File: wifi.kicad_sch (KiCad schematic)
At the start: 24 parts, among them P2 USB_C_Receptacle_USB2.0_16P, Q1 2N7002, U7 SC16C550BIBS, U8 ESP32-C3-WROOM-02, Y1 24 MHz

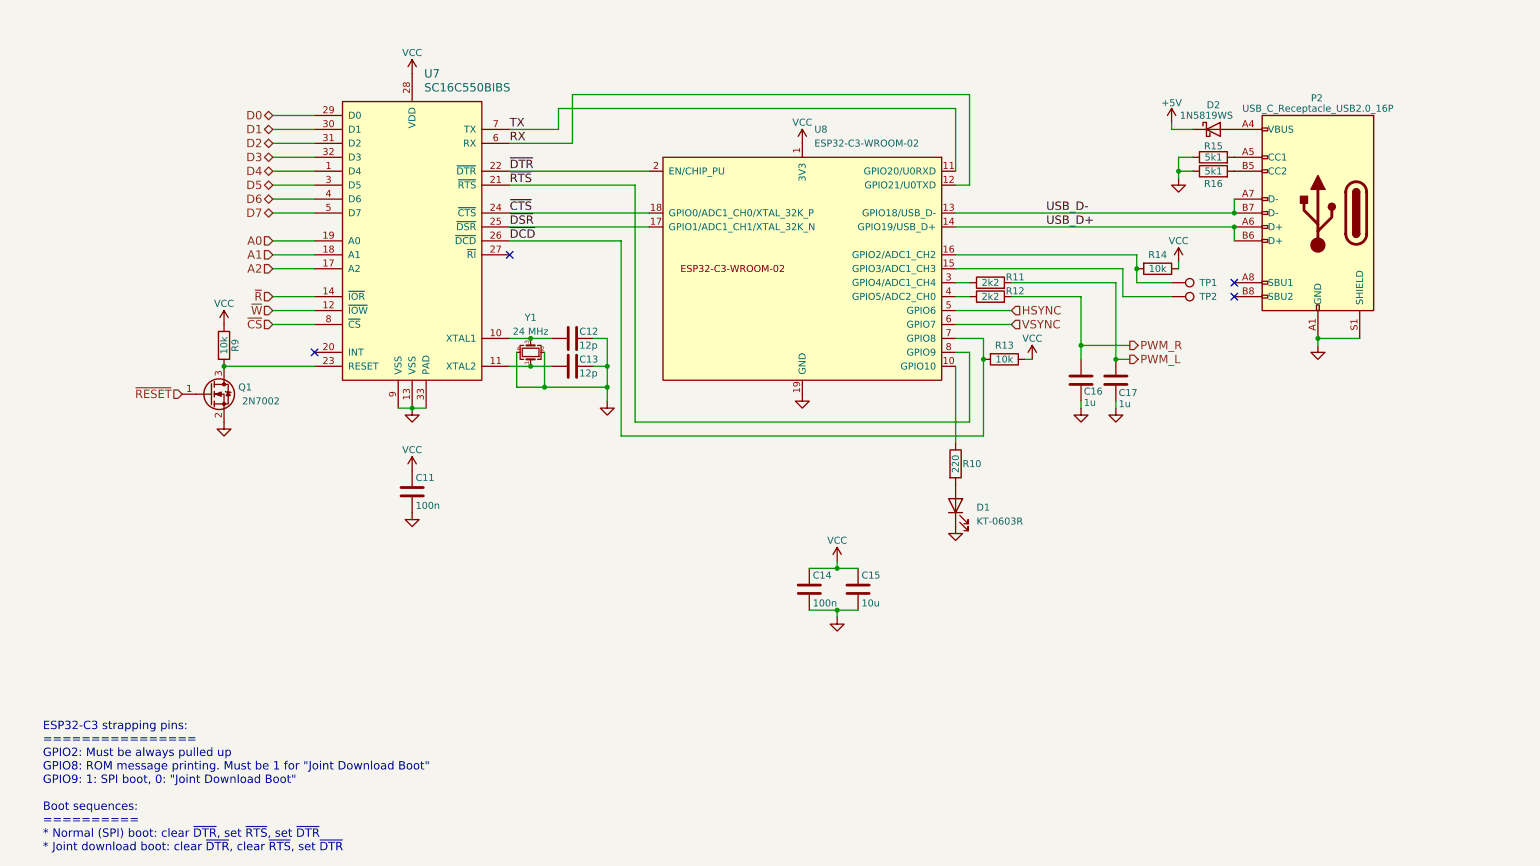
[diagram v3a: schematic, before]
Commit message: Allow ESP32 to reset the host
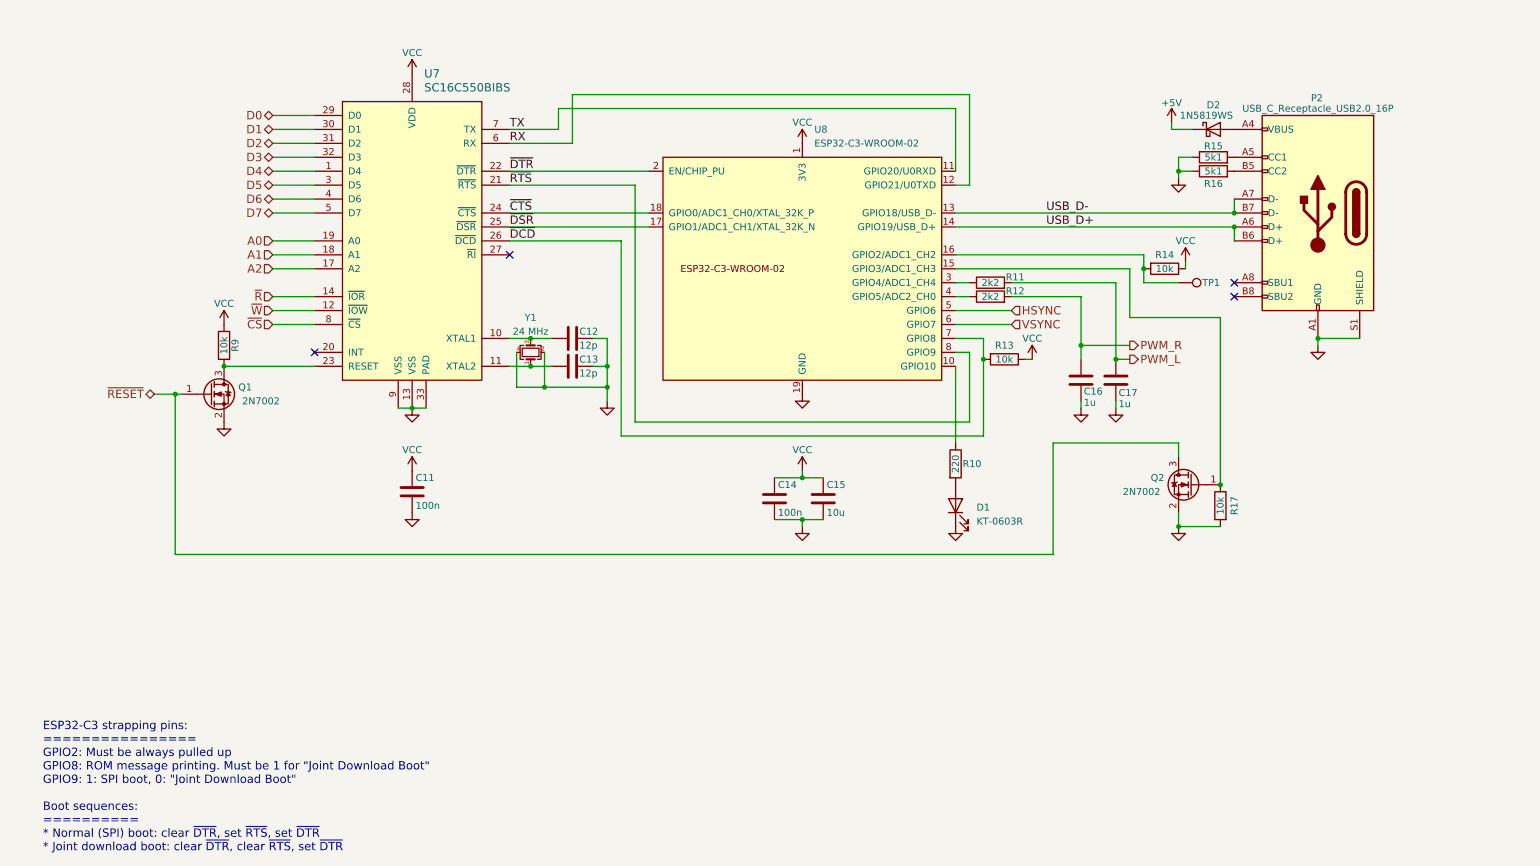
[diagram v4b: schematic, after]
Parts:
- removed TP2: TestPoint, TestPoint:TestPoint_Pad_D1.0mm, symbol Connector:TestPoint
- added Q2: 2N7002, Package_TO_SOT_SMD:SOT-23, symbol Device:Q_NMOS_GSD
- added R17: 10k, Resistor_SMD:R_0603_1608Metric, symbol Device:R
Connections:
- net GND: now also Q2.2 (S), R17.2
- net ~{RESET}: now also Q2.3 (D)
- net at U8.15 (GPIO3/ADC1_CH3): now also Q2.1 (G), R17.1
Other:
- moved on the sheet: C14, C15, R14, TP1
